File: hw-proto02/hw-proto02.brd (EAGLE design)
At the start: 54.3 x 62.2 mm, 25 parts, among them IC3 MCP2562T, IC5 IR4427S, J1 000, J2 000, Q1 SQJ147ELP-T1_GE3, Q2 SQJ147ELP-T1_GE3

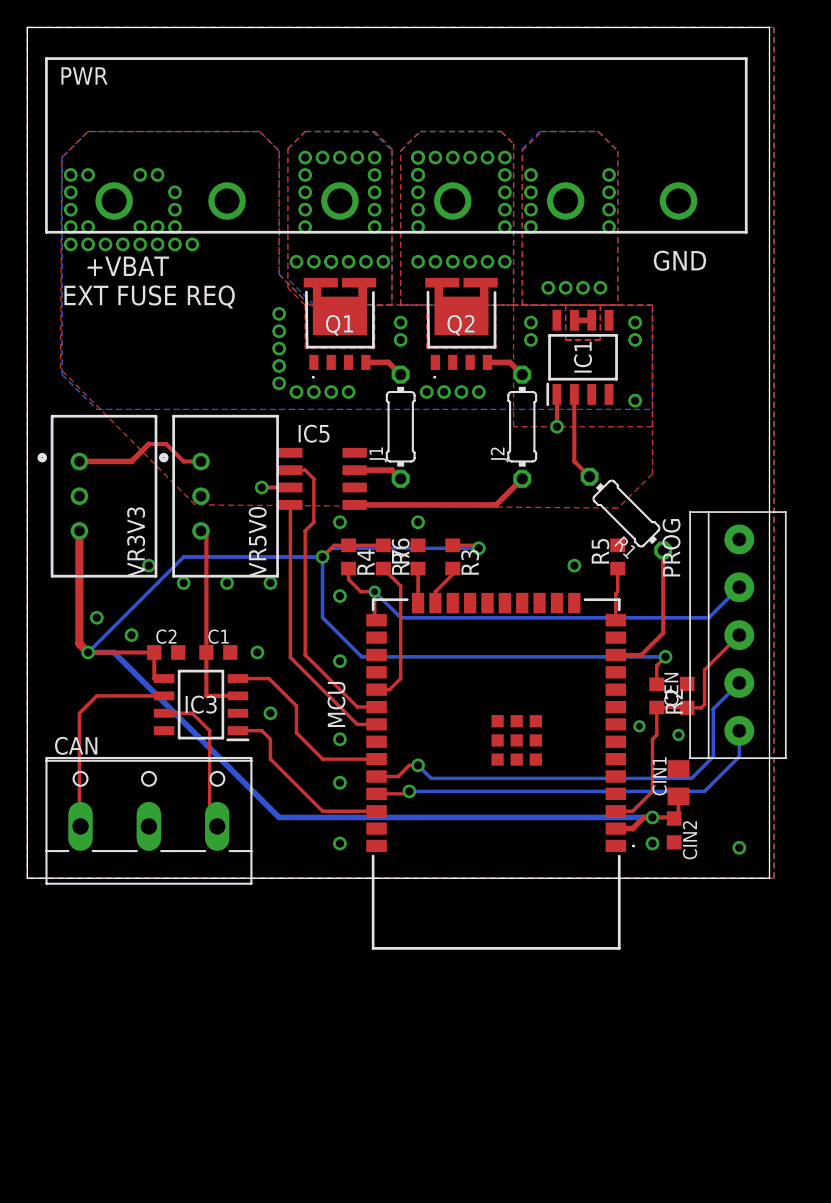
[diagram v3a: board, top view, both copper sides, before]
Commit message: updated mosfet driver
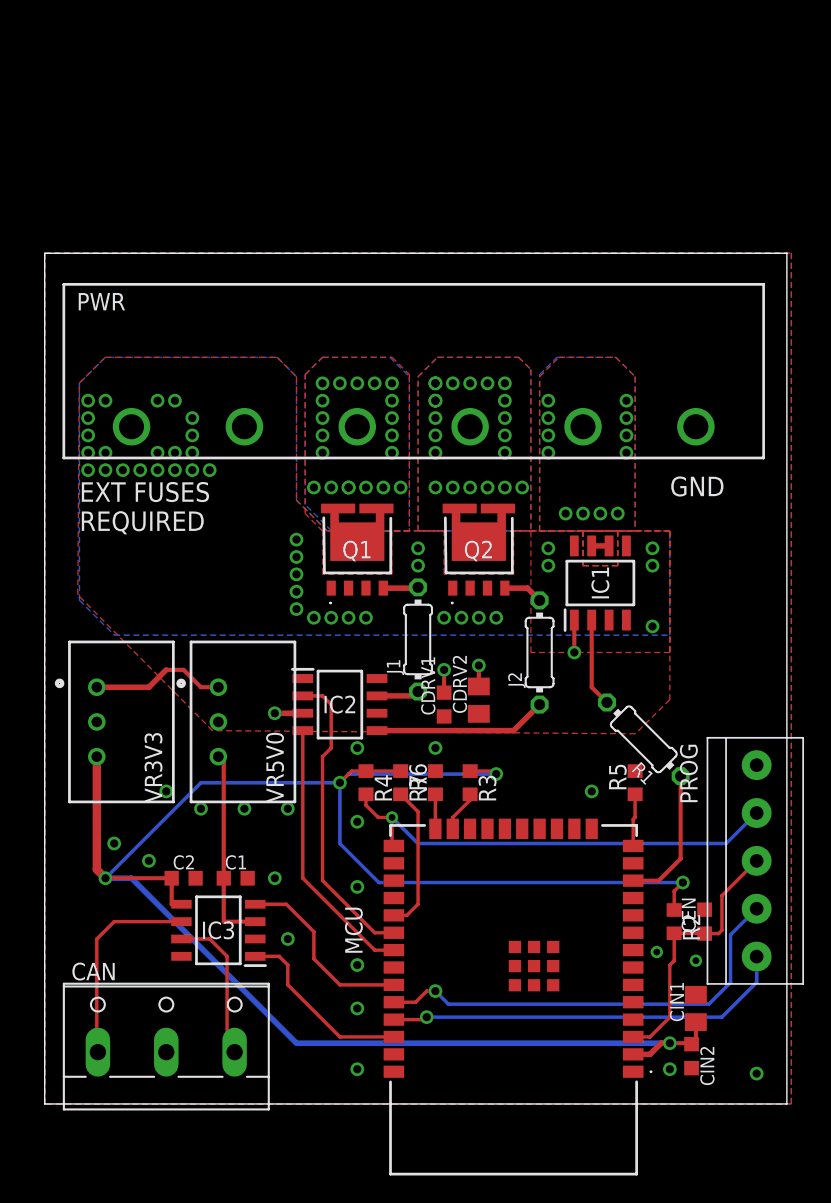
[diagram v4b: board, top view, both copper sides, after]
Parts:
- removed IC5: IR4427S, ir:SO08
- added CDRV1: 100n, rcl:C0603K
- added CDRV2: 4u7, rcl:C0805K
- added IC2: UCC27523DR, UCC27523DR-fet-driver:SOIC127P600X175-8N
- J1, J2: value 000 -> 10
- R1: value 10K0 -> 100
- moved IC1 16.6 mm to (41.9, 39.4)
- moved PWR 16.6 mm to (7.62, 50.8)
- moved Q1 16.6 mm to (24.1, 41.9)
- moved Q2 16.6 mm to (33.0, 41.9)
- moved CIN2 16.6 mm to (48.6, 4.76)
- moved PROG 16.6 mm to (53.3, 19.1)
- moved R1 16.6 mm to (45.1, 27.9)
- moved C1 16.6 mm to (15.2, 17.8)
- moved C2 16.6 mm to (11.4, 17.8)
- moved CAN 16.6 mm to (10.2, 6.35)
- moved CEN 16.6 mm to (49.5, 14.6)
- moved CIN1 16.6 mm to (48.9, 8.26)
- moved IC3 16.6 mm to (14.0, 14.0)
- moved J2 16.6 mm to (37.5, 34.3)
- moved MCU 16.6 mm to (35.6, 8.89)
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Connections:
- net +12V: now also CDRV1.1, CDRV2.1, IC2.6; no longer IC5.6
- net CTL1: now also IC2.2; no longer IC5.2
- net CTL2: now also IC2.4; no longer IC5.4
- net GND: now also CDRV1.2, CDRV2.2, IC2.3; no longer IC5.3
- net N$3: now also IC2.5; no longer IC5.5
- net N$4: now also IC2.7; no longer IC5.7
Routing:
- net GND: track 4.46 -> 7.62 mm, vias 22 -> 24
- net SW2: vias 22 -> 21
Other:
- board text added: "EXT FUSES REQUIRED"
- board text removed: "+VBAT EXT FUSE REQ"

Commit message: grounded can connector, layout tweaks
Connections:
- net GND: now also CAN.2
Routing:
- net GND: vias 24 -> 45
- net +12V: vias 41 -> 60
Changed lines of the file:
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@@
 <layers>
 <layer number="1" name="Top" color="4" fill="1" visible="yes" active="yes"/>
-<layer number="16" name="Bottom" color="1" fill="1" visible="no" active="yes"/>
+<layer number="16" name="Bottom" color="1" fill="1" visible="yes" active="yes"/>
 <layer number="17" name="Pads" color="2" fill="1" visible="yes" active="yes"/>
 <layer number="18" name="Vias" color="2" fill="1" visible="yes" active="yes"/>
@@
 <board>
 <plain>
-<wire x1="1.27" y1="1.27" x2="55.55" y2="1.27" width="0" layer="20"/>
-<wire x1="55.55" y1="1.27" x2="55.55" y2="63.49" width="0" layer="20"/>
-<wire x1="55.55" y1="63.49" x2="1.27" y2="63.49" width="0" layer="20"/>
-<wire x1="1.27" y1="63.49" x2="1.27" y2="1.27" width="0" layer="20"/>
+<wire x1="1.27" y1="1.27" x2="55.55" y2="1.27" width="0.254" layer="20"/>
+<wire x1="55.55" y1="1.27" x2="55.55" y2="63.49" width="0.254" layer="20"/>
+<wire x1="55.55" y1="63.49" x2="1.27" y2="63.49" width="0.254" layer="20"/>
+<wire x1="1.27" y1="63.49" x2="1.27" y2="1.27" width="0.254" layer="20"/>
 <text x="3.81" y="43.18" size="1.4224" layer="25" font="vector" ratio="14">EXT FUSES
 REQUIRED</text>
@@
 </polygon>
 <via x="38.1" y="52.705" extent="1-16" drill="0.6"/>
-<via x="43.815" y="52.705" extent="1-16" drill="0.6"/>
-<via x="43.815" y="51.435" extent="1-16" drill="0.6"/>
-<via x="43.815" y="50.165" extent="1-16" drill="0.6"/>
-<via x="43.815" y="48.895" extent="1-16" drill="0.6"/>
+<via x="43.18" y="52.705" extent="1-16" drill="0.6"/>
+<via x="43.18" y="51.435" extent="1-16" drill="0.6"/>
+<via x="43.18" y="50.165" extent="1-16" drill="0.6"/>
+<via x="43.18" y="48.895" extent="1-16" drill="0.6"/>
 <via x="38.1" y="48.895" extent="1-16" drill="0.6"/>
 <via x="39.37" y="44.45" extent="1-16" drill="0.6"/>
@@
 <wire x1="30.48" y1="33.02" x2="30.48" y2="31.355" width="0.3048" layer="1"/>
 <wire x1="33.02" y1="33.3375" x2="33.02" y2="31.7975" width="0.3048" layer="1"/>
+<via x="46.355" y="48.895" extent="1-16" drill="0.6"/>
+<via x="46.355" y="50.165" extent="1-16" drill="0.6"/>
+<via x="46.355" y="51.435" extent="1-16" drill="0.6"/>
+<via x="46.355" y="52.705" extent="1-16" drill="0.6"/>
+<via x="51.435" y="52.705" extent="1-16" drill="0.6"/>
+<via x="51.435" y="51.435" extent="1-16" drill="0.6"/>
+<via x="51.435" y="50.165" extent="1-16" drill="0.6"/>
+<via x="51.435" y="48.895" extent="1-16" drill="0.6"/>
+<via x="42.2275" y="18.7325" extent="1-16" drill="0.6"/>
+<via x="29.845" y="18.7325" extent="1-16" drill="0.6"/>
+<via x="46.0375" y="19.05" extent="1-16" drill="0.6"/>
+<via x="46.0375" y="21.59" extent="1-16" drill="0.6"/>
+<via x="29.21" y="3.81" extent="1-16" drill="0.6"/>
+<via x="41.91" y="3.81" extent="1-16" drill="0.6"/>
+<via x="41.91" y="10.16" extent="1-16" drill="0.6"/>
+<via x="29.21" y="11.43" extent="1-16" drill="0.6"/>
+<via x="53.34" y="7.62" extent="1-16" drill="0.6"/>
+<via x="49.53" y="17.78" extent="1-16" drill="0.6"/>
+<via x="49.53" y="21.59" extent="1-16" drill="0.6"/>
+<via x="6.35" y="12.7" extent="1-16" drill="0.6"/>
+<via x="8.89" y="12.7" extent="1-16" drill="0.6"/>
+<contactref element="CAN" pad="2"/>
 </signal>
 <signal name="SW1">
@@
 <vertex x="36.83" y="34.29"/>
 </polygon>
-<via x="4.445" y="52.705" extent="1-16" drill="0.6"/>
-<via x="5.715" y="52.705" extent="1-16" drill="0.6"/>
-<via x="9.525" y="52.705" extent="1-16" drill="0.6"/>
-<via x="10.795" y="52.705" extent="1-16" drill="0.6"/>
-<via x="12.065" y="51.435" extent="1-16" drill="0.6"/>
-<via x="12.065" y="50.165" extent="1-16" drill="0.6"/>
-<via x="4.445" y="51.435" extent="1-16" drill="0.6"/>
-<via x="4.445" y="50.165" extent="1-16" drill="0.6"/>
-<via x="4.445" y="48.895" extent="1-16" drill="0.6"/>
-<via x="5.715" y="48.895" extent="1-16" drill="0.6"/>
-<via x="9.525" y="48.895" extent="1-16" drill="0.6"/>
-<via x="10.795" y="48.895" extent="1-16" drill="0.6"/>
-<via x="12.065" y="48.895" extent="1-16" drill="0.6"/>
+<via x="4.7625" y="52.705" extent="1-16" drill="0.6"/>
+<via x="18.7325" y="51.435" extent="1-16" drill="0.6"/>
+<via x="18.7325" y="50.165" extent="1-16" drill="0.6"/>
+<via x="18.7325" y="48.895" extent="1-16" drill="0.6"/>
+<via x="4.7625" y="51.435" extent="1-16" drill="0.6"/>
+<via x="4.7625" y="50.165" extent="1-16" drill="0.6"/>
+<via x="4.7625" y="48.895" extent="1-16" drill="0.6"/>
 <polygon width="0.4064" layer="16" spacing="0.3048" isolate="0.254" thermals="no" rank="4">
 <vertex x="18.265096875" y="55.88"/>
@@
 <via x="45.72" y="36.195" extent="1-16" drill="0.6"/>
 <via x="45.72" y="41.91" extent="1-16" drill="0.6"/>
-<via x="4.445" y="47.625" extent="1-16" drill="0.6"/>
-<via x="5.715" y="47.625" extent="1-16" drill="0.6"/>
-<via x="6.985" y="47.625" extent="1-16" drill="0.6"/>
-<via x="8.255" y="47.625" extent="1-16" drill="0.6"/>
-<via x="9.525" y="47.625" extent="1-16" drill="0.6"/>
-<via x="10.795" y="47.625" extent="1-16" drill="0.6"/>
-<via x="12.065" y="47.625" extent="1-16" drill="0.6"/>
-<via x="13.335" y="47.625" extent="1-16" drill="0.6"/>
+<via x="4.7625" y="47.625" extent="1-16" drill="0.6"/>
+<via x="6.0325" y="47.625" extent="1-16" drill="0.6"/>
+<via x="7.3025" y="47.625" extent="1-16" drill="0.6"/>
+<via x="8.5725" y="47.625" extent="1-16" drill="0.6"/>
+<via x="9.8425" y="47.625" extent="1-16" drill="0.6"/>
+<via x="11.1125" y="47.625" extent="1-16" drill="0.6"/>
+<via x="12.3825" y="47.625" extent="1-16" drill="0.6"/>
+<via x="13.6525" y="47.625" extent="1-16" drill="0.6"/>
 <wire x1="5.08" y1="31.75" x2="8.89" y2="31.75" width="0.4064" layer="1"/>
 <wire x1="8.89" y1="31.75" x2="10.16" y2="33.02" width="0.4064" layer="1"/>
@@
 <contactref element="CDRV1" pad="1"/>
 <contactref element="CDRV2" pad="1"/>
+<via x="14.9225" y="47.625" extent="1-16" drill="0.6"/>
+<via x="16.1925" y="47.625" extent="1-16" drill="0.6"/>
+<via x="17.4625" y="47.625" extent="1-16" drill="0.6"/>
+<via x="18.7325" y="47.625" extent="1-16" drill="0.6"/>
+<via x="11.1125" y="48.895" extent="1-16" drill="0.6"/>
+<via x="11.1125" y="50.165" extent="1-16" drill="0.6"/>
+<via x="11.1125" y="51.435" extent="1-16" drill="0.6"/>
+<via x="11.1125" y="52.705" extent="1-16" drill="0.6"/>
+<via x="12.3825" y="52.705" extent="1-16" drill="0.6"/>
+<via x="12.3825" y="51.435" extent="1-16" drill="0.6"/>
+<via x="12.3825" y="50.165" extent="1-16" drill="0.6"/>
+<via x="12.3825" y="48.895" extent="1-16" drill="0.6"/>
+<via x="4.7625" y="53.975" extent="1-16" drill="0.6"/>
+<via x="6.0325" y="53.975" extent="1-16" drill="0.6"/>
+<via x="7.3025" y="53.975" extent="1-16" drill="0.6"/>
+<via x="8.5725" y="53.975" extent="1-16" drill="0.6"/>
+<via x="9.8425" y="53.975" extent="1-16" drill="0.6"/>
+<via x="11.1125" y="53.975" extent="1-16" drill="0.6"/>
+<via x="12.3825" y="53.975" extent="1-16" drill="0.6"/>
+<via x="13.6525" y="53.975" extent="1-16" drill="0.6"/>
+<via x="14.9225" y="53.975" extent="1-16" drill="0.6"/>
+<via x="16.1925" y="53.975" extent="1-16" drill="0.6"/>
+<via x="17.4625" y="53.975" extent="1-16" drill="0.6"/>
+<via x="18.7325" y="53.975" extent="1-16" drill="0.6"/>
+<via x="18.7325" y="52.705" extent="1-16" drill="0.6"/>
 </signal>
 <signal name="+5V">
